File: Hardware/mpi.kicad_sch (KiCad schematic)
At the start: 21 parts, among them J22 J-0530471010, J23 J-0532610471, U6 U-MAX3378EEUD+T, U7 MAX3086EESD+T

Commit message: Assign footprints
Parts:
- C49, C50, C51, C52: footprint 0603 -> Capacitor_SMD:C_0603_1608Metric
- J22: footprint J-0530471010 -> CTS-SAT-1:J-0530471010
- J23: footprint J-53261-0471 -> CTS-SAT-1:J-53261-0471
- R87, R88, R89, R90, R91, R92, R93, R94, R95, R96, R97, R98, R99: footprint 0603 -> Resistor_SMD:R_0603_1608Metric
- U6: footprint C__Users_James_Documents_Calgary to Space_OBC_PCB_hardware_OBC Development Board_OBC Development Board.PcbLib:U-MAX3378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 -> CTS-SAT-1:U-MAX3378EEUD+T
- U7: footprint U-MAX3086EESD+T -> CTS-SAT-1:U-MAX3086EESD+T
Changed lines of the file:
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@@
 			)
 		)
-		(property "Footprint" "0603"
+		(property "Footprint" "Resistor_SMD:R_0603_1608Metric"
 			(at 238.76 80.01 0)
 			(effects
@@
 			)
 		)
-		(property "Footprint" "0603"
+		(property "Footprint" "Resistor_SMD:R_0603_1608Metric"
 			(at 87.63 106.68 0)
 			(effects
@@
 			)
 		)
-		(property "Footprint" "C__Users_James_Documents_Calgary to Space_OBC_PCB_hardware_OBC Development Board_OBC Development Board.PcbLib:U-MAX3378EEUD+T"
+		(property "Footprint" "CTS-SAT-1:U-MAX3378EEUD+T"
 			(at 110.49 78.74 0)
 			(effects
@@
 			)
 		)
-		(property "Footprint" "J-53261-0471"
+		(property "Footprint" "CTS-SAT-1:J-53261-0471"
 			(at 153.67 171.45 0)
 			(effects
@@
 			)
 		)
-		(property "Footprint" "0603"
+		(property "Footprint" "Capacitor_SMD:C_0603_1608Metric"
 			(at 130.81 52.07 0)
 			(effects
@@
 			)
 		)
-		(property "Footprint" "0603"
+		(property "Footprint" "Capacitor_SMD:C_0603_1608Metric"
 			(at 198.12 54.61 0)
 			(effects
@@
 			)
 		)
-		(property "Footprint" "0603"
+		(property "Footprint" "Resistor_SMD:R_0603_1608Metric"
 			(at 81.28 91.44 0)
 			(effects
@@
 			)
 		)
-		(property "Footprint" "U-MAX3086EESD+T"
+		(property "Footprint" "CTS-SAT-1:U-MAX3086EESD+T"
 			(at 160.02 77.47 0)
 			(effects
@@
 			)
 		)
-		(property "Footprint" "0603"
+		(property "Footprint" "Resistor_SMD:R_0603_1608Metric"
 			(at 238.76 90.17 0)
 			(effects
@@
 			)
 		)
-		(property "Footprint" "0603"
+		(property "Footprint" "Resistor_SMD:R_0603_1608Metric"
 			(at 160.02 60.96 0)
 			(effects
@@
 			)
 		)
-		(property "Footprint" "0603"
+		(property "Footprint" "Resistor_SMD:R_0603_1608Metric"
 			(at 76.2 88.9 0)
 			(effects
@@
 			)
 		)
-		(property "Footprint" "0603"
+		(property "Footprint" "Resistor_SMD:R_0603_1608Metric"
 			(at 160.02 57.15 0)
 			(effects
@@
 			)
 		)
-		(property "Footprint" "0603"
+		(property "Footprint" "Resistor_SMD:R_0603_1608Metric"
 			(at 87.63 109.22 0)
 			(effects
@@
 			)
 		)
-		(property "Footprint" "0603"
+		(property "Footprint" "Capacitor_SMD:C_0603_1608Metric"
 			(at 96.52 52.07 0)
 			(effects
@@
 			)
 		)
-		(property "Footprint" "0603"
+		(property "Footprint" "Resistor_SMD:R_0603_1608Metric"
 			(at 76.2 83.82 0)
 			(effects
@@
 			)
 		)
-		(property "Footprint" "0603"
+		(property "Footprint" "Resistor_SMD:R_0603_1608Metric"
 			(at 193.04 105.41 0)
 			(effects
@@
 			)
 		)
-		(property "Footprint" "0603"
+		(property "Footprint" "Resistor_SMD:R_0603_1608Metric"
 			(at 238.76 85.09 0)
 			(effects
@@
 			)
 		)
-		(property "Footprint" "0603"
+		(property "Footprint" "Capacitor_SMD:C_0603_1608Metric"
 			(at 120.65 59.69 0)
 			(effects
@@
 			)
 		)
-		(property "Footprint" "J-0530471010"
+		(property "Footprint" "CTS-SAT-1:J-0530471010"
 			(at 114.3 166.37 0)
 			(effects
@@
 			)
 		)
-		(property "Footprint" "0603"
+		(property "Footprint" "Resistor_SMD:R_0603_1608Metric"
 			(at 160.02 53.34 0)
 			(effects
@@
 			)
 		)
-		(property "Footprint" "0603"
+		(property "Footprint" "Resistor_SMD:R_0603_1608Metric"
 			(at 76.2 86.36 0)
 			(effects

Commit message: make most changes from design review
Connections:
- net MOSI_MPI_TX_EN: now also R89.2; no longer R89.1
- net at U6.4 (IO_VL3): now also R89.1; no longer R89.2
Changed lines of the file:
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@@
 	(symbol
 		(lib_id "OBC Development Board:root_2_mirrored_RT-22R0-F-1/16W-0603_OBC Development Board.SchLib")
-		(at 76.2 88.9 0)
+		(at 81.28 88.9 0)
+		(mirror y)
 		(unit 1)
 		(exclude_from_sim no)
@@
 		(dnp no)
 		(property "Reference" "R89"
-			(at 81.28 88.9 0)
+			(at 76.2 88.9 0)
 			(effects
 				(font
@@
 		)
 		(property "Value" "22R"
-			(at 75.692 88.138 0)
+			(at 81.788 88.138 0)
 			(effects
 				(font
@@
 		)
 		(property "Footprint" "Resistor_SMD:R_0603_1608Metric"
-			(at 76.2 88.9 0)
+			(at 81.28 88.9 0)
 			(effects
 				(font
@@
 		)
 		(property "Datasheet" ""
-			(at 76.2 88.9 0)
+			(at 81.28 88.9 0)
 			(effects
 				(font
@@
 		)
 		(property "Description" "22 Ohms ±0.5% 0.063W, 1/16W Chip Resistor 0603 (1608 Metric) - Thin Film"
-			(at 76.2 88.9 0)
+			(at 81.28 88.9 0)
 			(effects
 				(font
@@
 		)
 		(property "COMPONENTLINK1DESCRIPTION" "Datasheet"
-			(at 75.692 88.138 0)
+			(at 81.788 88.138 0)
 			(effects
 				(font
@@
 		)
 		(property "COMPONENTLINK1URL" "https://www.vishay.com/docs/20035/dcrcwe3.pdf"
-			(at 75.692 88.138 0)
+			(at 81.788 88.138 0)
 			(effects
 				(font
@@
 		)
 		(property "COMPONENTLINK2DESCRIPTION" "Manufacturer Website"
-			(at 75.692 88.138 0)
+			(at 81.788 88.138 0)
 			(effects
 				(font
@@
 		)
 		(property "DISTRIBUTOR" "Digikey"
-			(at 75.692 88.138 0)
+			(at 81.788 88.138 0)
 			(effects
 				(font
@@
 		)
 		(property "DISTRIBUTOR PART #" "RR08Q22DCT-ND"
-			(at 75.692 88.138 0)
+			(at 81.788 88.138 0)
 			(effects
 				(font
@@
 		)
 		(property "MANUFACTURER" "Susumu"
-			(at 75.692 88.138 0)
+			(at 81.788 88.138 0)
 			(effects
 				(font
@@
 		)
 		(property "MANUFACTURER PART #" "RR0816Q-220-D"
-			(at 75.692 88.138 0)
+			(at 81.788 88.138 0)
 			(effects
 				(font
@@
 		)
 		(property "PART DESCRIPTION" "22 Ohms ±0.5% 0.063W, 1/16W Chip Resistor 0603 (1608 Metric) - Thin Film"
-			(at 75.692 88.138 0)
+			(at 81.788 88.138 0)
 			(effects
 				(font
@@
 		)
 		(property "COMPONENTLINK2URL" "https://www.vishay.com/"
-			(at 75.692 88.138 0)
+			(at 81.788 88.138 0)
 			(effects
 				(font
@@
 		)
 		(property "ALTIUM_VALUE" "22R"
-			(at 72.39 88.9 0)
+			(at 85.09 88.9 0)
 			(effects
 				(font

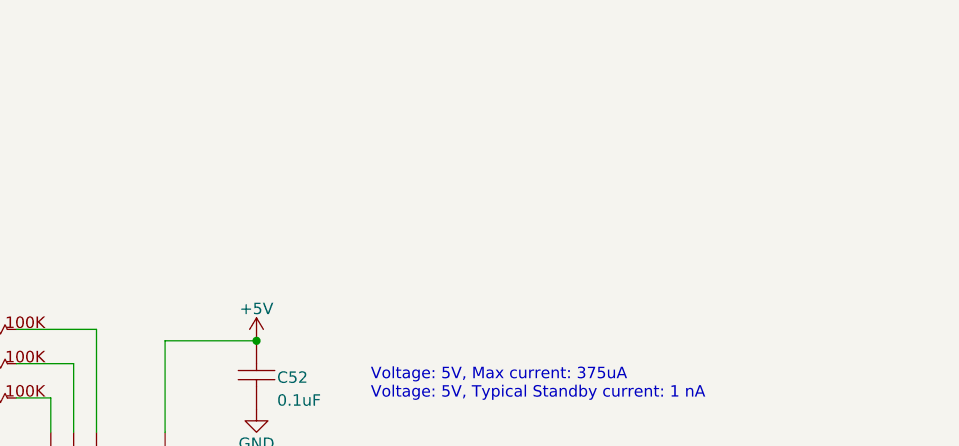
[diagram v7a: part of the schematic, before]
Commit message: H1/2 capacitors and LEDs
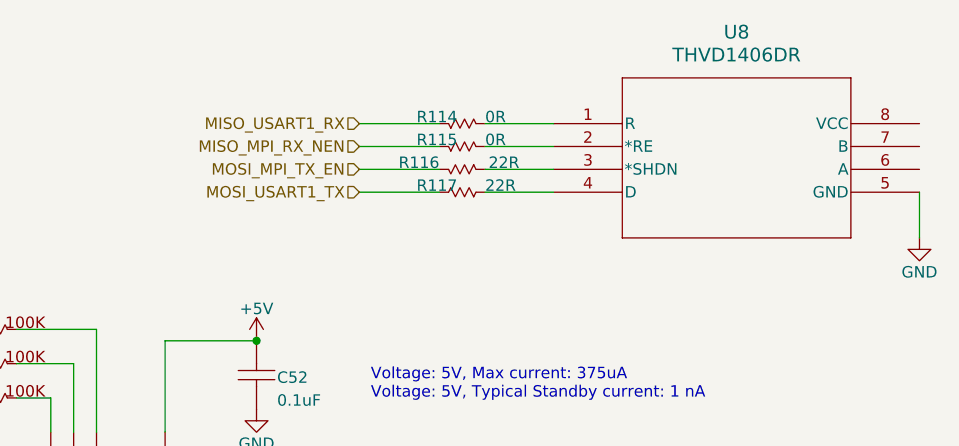
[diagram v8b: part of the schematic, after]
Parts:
- added R114, R115: 0R, Resistor_SMD:R_0603_1608Metric, symbol OBC Development Board:root_0_RT-0R00-F-1/10W-0603_OBC Development Board.SchLib
- added R116: 22R, Resistor_SMD:R_0603_1608Metric, symbol OBC Development Board:root_2_mirrored_RT-22R0-F-1/16W-0603_OBC Development Boar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
- added R117: 22R, Resistor_SMD:R_0603_1608Metric, symbol OBC Development Board:root_0_mirrored_RT-22R0-F-1/16W-0603_OBC Development Boar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
- added U8: THVD1406DR, SOIC_D0008A_TEX, symbol THVD1406DR:THVD1406DR
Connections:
- net GND: now also U8.5 (GND)
- net MISO_MPI_RX_NEN: now also R115.1
- net MISO_USART1_RX: now also R114.1
- net MOSI_MPI_TX_EN: now also R116.2
- net MOSI_USART1_TX: now also R117.2
- new net: R115.2, U8.2 (*RE)
- new net: R117.1, U8.4 (D)
- new net: R116.1, U8.3 (*SHDN)
- new net: R114.2, U8.1 (R)
